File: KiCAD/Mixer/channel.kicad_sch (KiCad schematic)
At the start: 0 parts

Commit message: Power Bus, Footprints, Audio Bus
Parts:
- added J2: Conn_02x05_Odd_Even, Connector_PinHeader_2.54mm:PinHeader_2x05_P2.54mm_Vertical, symbol Connector_Generic:Conn_02x05_Odd_Even
- added J3: Conn_02x03_Odd_Even, Connector_PinHeader_2.54mm:PinHeader_2x03_P2.54mm_Vertical, symbol Connector_Generic:Conn_02x03_Odd_Even
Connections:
- net GND: now also J2.5 (Pin_5), J2.6 (Pin_6), J3.3 (Pin_3), J3.4 (Pin_4)
- new net ch1out_L: J2.1 (Pin_1), J2.2 (Pin_2)
- new net ch1out_R: J2.10 (Pin_10), J2.9 (Pin_9)
- new net ch1send_L: J3.1 (Pin_1), J3.2 (Pin_2)
- new net ch1send_R: J3.5 (Pin_5), J3.6 (Pin_6)
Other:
- added sheet Channel Power (ch_power.kicad_sch)
- sheet Inputs ports: added GND; removed none
- note added: "Audio Output Bus"

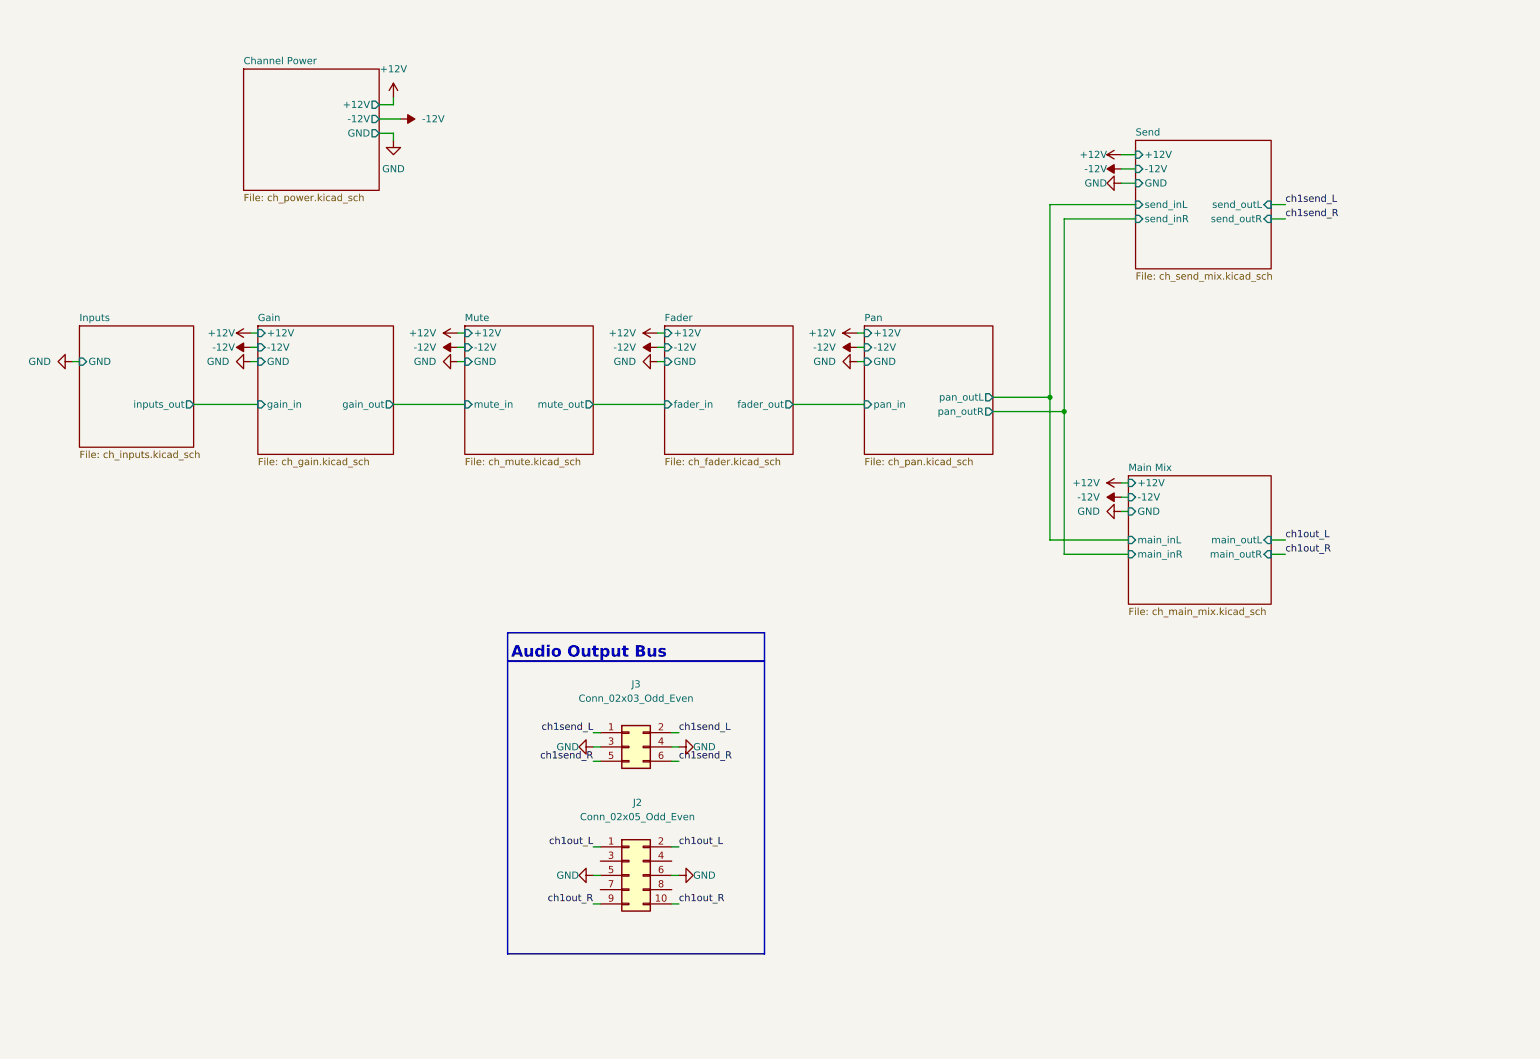
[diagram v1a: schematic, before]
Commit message: added second channel and footprints / created PCB desing...might make PCB bit bigger
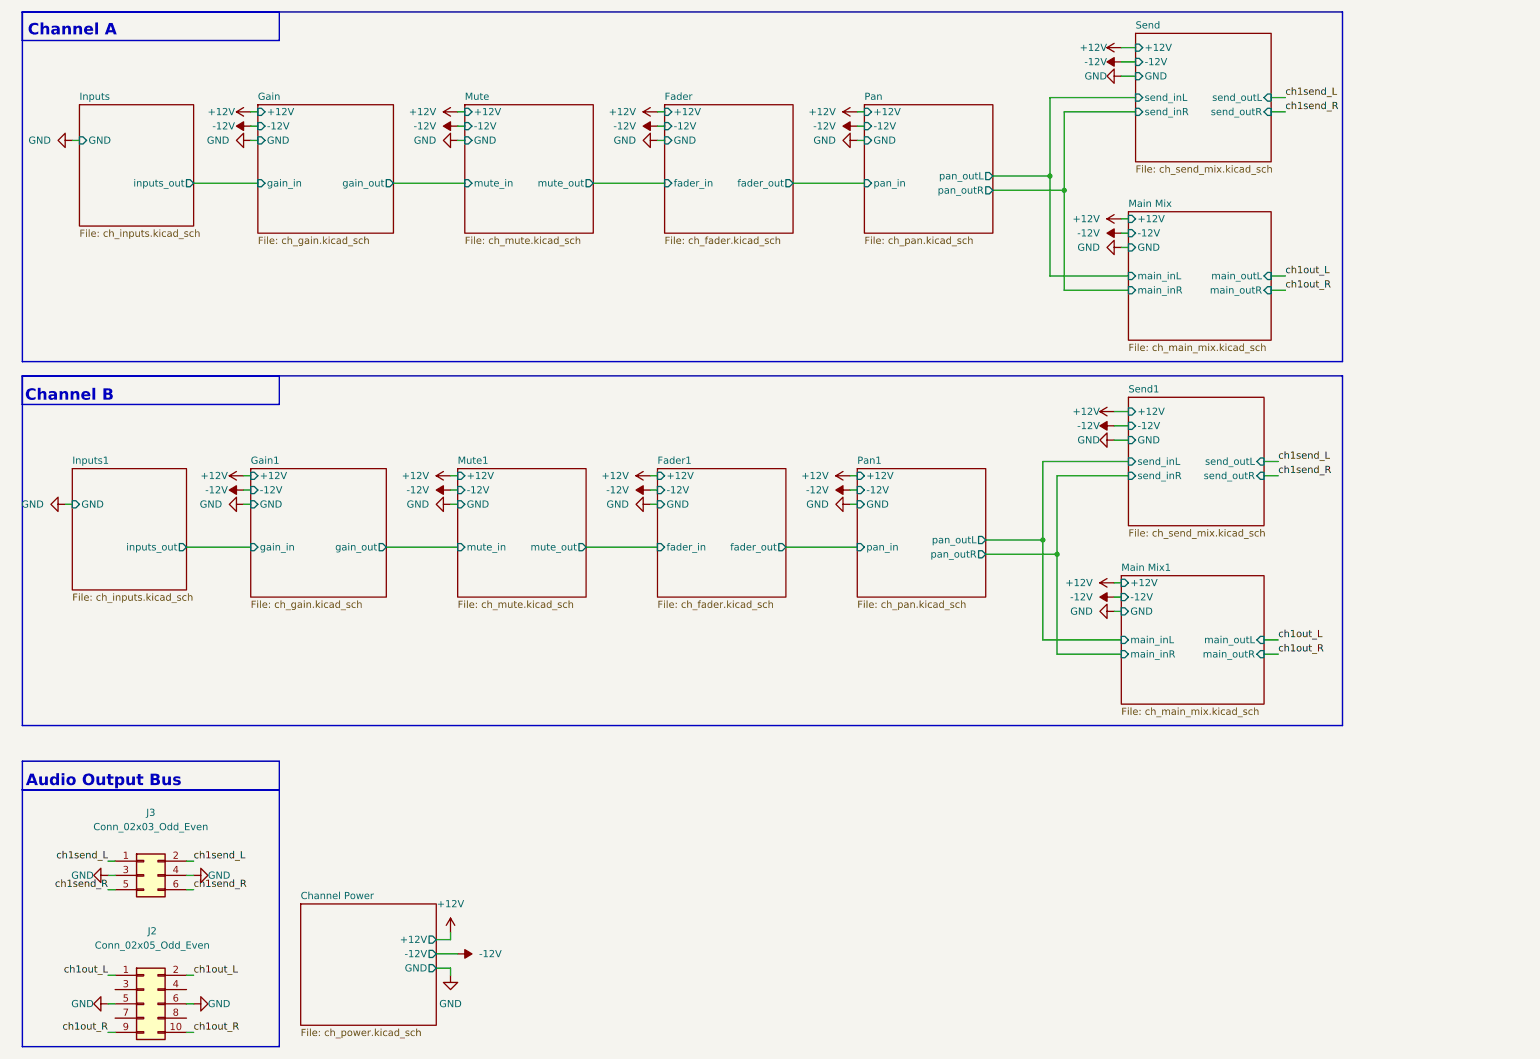
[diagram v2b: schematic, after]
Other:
- added sheet Fader1 (ch_fader.kicad_sch)
- added sheet Gain1 (ch_gain.kicad_sch)
- added sheet Inputs1 (ch_inputs.kicad_sch)
- added sheet Main Mix1 (ch_main_mix.kicad_sch)
- added sheet Mute1 (ch_mute.kicad_sch)
- added sheet Pan1 (ch_pan.kicad_sch)
- added sheet Send1 (ch_send_mix.kicad_sch)
- note added: "Channel A"
- note added: "Channel B"
- moved on the sheet: J2, J3

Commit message: Cs an OPV-Strom, Anpassung clicklessmute,...
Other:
- note added: "10u an die Versorgungspins OPVs Clipping Rs 10 zu 1 & Sockel"
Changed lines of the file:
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@@
+		)
+	)
+	(text "10u an die Versorgungspins \nOPVs\nClipping Rs 10 zu 1 & Sockel"
+		(exclude_from_sim no)
+		(at 120.396 153.416 0)
+		(effects
+			(font
+				(size 1.27 1.27)
+			)
+			(justify left)
 		)
 	)

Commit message: überarbeitete Schaltung und PCB Desing...v1.0 FERTIG
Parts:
- removed J2: Conn_02x05_Odd_Even, Connector_PinHeader_2.54mm:PinHeader_2x05_P2.54mm_Vertical, symbol Connector_Generic:Conn_02x05_Odd_Even
- removed J3: Conn_02x03_Odd_Even, Connector_PinHeader_2.54mm:PinHeader_2x03_P2.54mm_Vertical, symbol Connector_Generic:Conn_02x03_Odd_Even
- added J10, J11: Conn_02x09_Odd_Even, Connector_PinHeader_2.54mm:PinHeader_2x09_P2.54mm_Vertical, symbol Connector_Generic:Conn_02x09_Odd_Even
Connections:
- net GND: now also J10.13 (Pin_13), J10.14 (Pin_14), J10.3 (Pin_3), J10.4 (Pin_4), J10.7 (Pin_7), J10.8 (Pin_8), J11.13 (Pin_13), J11.14 (Pin_14), J11.3 (Pin_3), J11.4 (Pin_4), J11.7 (Pin_7), J11.8 (Pin_8)
- new net main_mixL: J10.1 (Pin_1), J10.2 (Pin_2)
- new net main_mixR: J10.5 (Pin_5), J10.6 (Pin_6)
- new net pre_mixL: J11.1 (Pin_1), J11.2 (Pin_2)
- new net pre_mixR: J11.5 (Pin_5), J11.6 (Pin_6)
- new net pre_send1L: J11.10 (Pin_10), J11.9 (Pin_9)
- new net pre_send1R: J11.11 (Pin_11), J11.12 (Pin_12)
- new net pre_send2L: J11.15 (Pin_15), J11.16 (Pin_16)
- new net pre_send2R: J11.17 (Pin_17), J11.18 (Pin_18)
- new net send_out1L: J10.10 (Pin_10), J10.9 (Pin_9)
- new net send_out1R: J10.11 (Pin_11), J10.12 (Pin_12)
- new net send_out2L: J10.15 (Pin_15), J10.16 (Pin_16)
- new net send_out2R: J10.17 (Pin_17), J10.18 (Pin_18)
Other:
- removed sheet Main Mix1
- removed sheet Send1
- sheet Main Mix ports: added main_inL1, main_inL2, main_inR1, main_inR2, pre_mixL, pre_mixR; removed main_inL, main_inR
- sheet Send ports: added pre_send1L, pre_send1R, pre_send2L, pre_send2R, send_inL1, send_inL2, send_inR1, send_inR2, send_out1L, send_out1R, send_out2L, send_out2R; removed send_inL, send_inR, send_outL, send_outR
- note added: "1opv_inv"
- note added: "4opv"
- note added: "8opv"
- note added: "Audio Input Bus"
- note added: "Channel 1"
- note added: "Channel 2"
- note added: "NICHT INVERTIERT ->"
- note removed: "Channel A"
- note removed: "Channel B"

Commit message: Rework of schematic, with error fixes and reworked pcb
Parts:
- renumbered J11 to J1, J10 to J2
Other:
- sheet Inputs1 renamed InputsL
- sheet Fader1: file ch_fader.kicad_sch -> ch_faderL.kicad_sch
- sheet Gain1: file ch_gain.kicad_sch -> ch_gainL.kicad_sch
- sheet Inputs ports: added +12V; removed none
- sheet InputsL: file ch_inputs.kicad_sch -> ch_inputsR.kicad_sch
- sheet InputsL ports: added +12V; removed none
- sheet Mute1: file ch_mute.kicad_sch -> ch_muteL.kicad_sch
- sheet Pan1: file ch_pan.kicad_sch -> ch_panL.kicad_sch
- moved on the sheet: J1, J2
